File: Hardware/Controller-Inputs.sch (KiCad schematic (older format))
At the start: 35 parts, among them J1 RJ45, U1 PC817, U2 PC817, U3 PC817, U4 PC817, U5 PC817, U6 PC817, U8 74HC14

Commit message: Add files via upload
HW layout and libs
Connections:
- wire segments 116 -> 115
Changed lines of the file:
@@
 LIBS:L298N
 LIBS:WS2812B
+LIBS:a4973
 LIBS:a3968
 LIBS:lm2675
@@
 $EndComp
 $Comp
-L GND #PWR09
+L GND #PWR08
 U 1 1 5A67C8BB
 P 5050 6000
-F 0 "#PWR09" H 5050 5750 50  0001 C CNN
+F 0 "#PWR08" H 5050 5750 50  0001 C CNN
 F 1 "GND" H 5055 5827 50  0000 C CNN
 F 2 "" H 5050 6000 50  0001 C CNN
@@
 $EndComp
 $Comp
-L GND #PWR011
+L GND #PWR09
 U 1 1 5A67C8F8
 P 4550 6250
-F 0 "#PWR011" H 4550 6000 50  0001 C CNN
+F 0 "#PWR09" H 4550 6000 50  0001 C CNN
 F 1 "GND" H 4555 6077 50  0000 C CNN
 F 2 "" H 4550 6250 50  0001 C CNN
@@
 $EndComp
 $Comp
-L GND #PWR012
+L GND #PWR010
 U 1 1 5A67C90A
 P 6400 5150
-F 0 "#PWR012" H 6400 4900 50  0001 C CNN
+F 0 "#PWR010" H 6400 4900 50  0001 C CNN
 F 1 "GND" H 6405 4977 50  0000 C CNN
 F 2 "" H 6400 5150 50  0001 C CNN
@@
 $EndComp
 $Comp
-L GND #PWR013
+L GND #PWR011
 U 1 1 5A67C917
 P 6450 6350
-F 0 "#PWR013" H 6450 6100 50  0001 C CNN
+F 0 "#PWR011" H 6450 6100 50  0001 C CNN
 F 1 "GND" H 6455 6177 50  0000 C CNN
 F 2 "" H 6450 6350 50  0001 C CNN
@@
 U 1 1 5A67C930
 P 6200 5800
-F 0 "R15" V 6407 5800 50  0000 C CNN
-F 1 "10K" V 6316 5800 50  0000 C CNN
+F 0 "R15" V 6100 5800 50  0000 C CNN
+F 1 "10K" V 6200 5800 50  0000 C CNN
 F 2 "Resistors_SMD:R_0805_HandSoldering" V 6130 5800 50  0001 C CNN
 F 3 "" H 6200 5800 50  0001 C CNN
@@
 U 1 1 5A67C937
 P 6150 4600
-F 0 "R13" V 6357 4600 50  0000 C CNN
-F 1 "10K" V 6266 4600 50  0000 C CNN
+F 0 "R13" V 6050 4600 50  0000 C CNN
+F 1 "10K" V 6150 4600 50  0000 C CNN
 F 2 "Resistors_SMD:R_0805_HandSoldering" V 6080 4600 50  0001 C CNN
 F 3 "" H 6150 4600 50  0001 C CNN
@@
 $EndComp
 $Comp
-L GND #PWR014
+L GND #PWR012
 U 1 1 5A67D6AF
 P 4200 1850
-F 0 "#PWR014" H 4200 1600 50  0001 C CNN
+F 0 "#PWR012" H 4200 1600 50  0001 C CNN
 F 1 "GND" H 4205 1677 50  0000 C CNN
 F 2 "" H 4200 1850 50  0001 C CNN
@@
 $EndComp
 $Comp
-L GND #PWR016
+L GND #PWR013
 U 1 1 5A67D6C7
 P 5050 2900
-F 0 "#PWR016" H 5050 2650 50  0001 C CNN
+F 0 "#PWR013" H 5050 2650 50  0001 C CNN
 F 1 "GND" H 5055 2727 50  0000 C CNN
 F 2 "" H 5050 2900 50  0001 C CNN
@@
 $EndComp
 $Comp
-L GND #PWR018
+L GND #PWR014
 U 1 1 5A67D6FD
 P 4550 3150
-F 0 "#PWR018" H 4550 2900 50  0001 C CNN
+F 0 "#PWR014" H 4550 2900 50  0001 C CNN
 F 1 "GND" H 4555 2977 50  0000 C CNN
 F 2 "" H 4550 3150 50  0001 C CNN
@@
 $EndComp
 $Comp
-L GND #PWR019
+L GND #PWR015
 U 1 1 5A67D70E
 P 6400 2050
-F 0 "#PWR019" H 6400 1800 50  0001 C CNN
+F 0 "#PWR015" H 6400 1800 50  0001 C CNN
 F 1 "GND" H 6405 1877 50  0000 C CNN
 F 2 "" H 6400 2050 50  0001 C CNN
@@
 $EndComp
 $Comp
-L GND #PWR020
+L GND #PWR016
 U 1 1 5A67D71A
 P 6450 3250
-F 0 "#PWR020" H 6450 3000 50  0001 C CNN
+F 0 "#PWR016" H 6450 3000 50  0001 C CNN
 F 1 "GND" H 6455 3077 50  0000 C CNN
 F 2 "" H 6450 3250 50  0001 C CNN
@@
 $EndComp
 $Comp
-L GND #PWR022
+L GND #PWR017
 U 1 1 5A67D72C
 P 9200 3600
-F 0 "#PWR022" H 9200 3350 50  0001 C CNN
+F 0 "#PWR017" H 9200 3350 50  0001 C CNN
 F 1 "GND" H 9205 3427 50  0000 C CNN
 F 2 "" H 9200 3600 50  0001 C CNN
@@
 U 1 1 5A67D732
 P 6200 2700
-F 0 "R14" V 6407 2700 50  0000 C CNN
-F 1 "10K" V 6316 2700 50  0000 C CNN
+F 0 "R14" V 6100 2700 50  0000 C CNN
+F 1 "10K" V 6200 2700 50  0000 C CNN
 F 2 "Resistors_SMD:R_0805_HandSoldering" V 6130 2700 50  0001 C CNN
 F 3 "" H 6200 2700 50  0001 C CNN
@@
 U 1 1 5A67D738
 P 6150 1500
-F 0 "R12" V 6357 1500 50  0000 C CNN
-F 1 "10K" V 6266 1500 50  0000 C CNN
+F 0 "R12" V 6050 1500 50  0000 C CNN
+F 1 "10K" V 6150 1500 50  0000 C CNN
 F 2 "Resistors_SMD:R_0805_HandSoldering" V 6080 1500 50  0001 C CNN
 F 3 "" H 6150 1500 50  0001 C CNN
@@
 Connection ~ 4200 1500
 Wire Wire Line
-	2650 2500 4350 2500
+	1650 2500 4350 2500
 Wire Wire Line
 	4350 2500 4350 2550
@@
 	6850 1750 6850 1800
 $Comp
-L GNDD #PWR023
+L GNDD #PWR018
 U 1 1 5A69E1AB
 P 2550 1850
-F 0 "#PWR023" H 2550 1600 50  0001 C CNN
+F 0 "#PWR018" H 2550 1600 50  0001 C CNN
 F 1 "GNDD" H 2550 1725 50  0000 C CNN
 F 2 "" H 2550 1850 50  0001 C CNN
@@
 	4050 2850 3900 2850
 $Comp
-L GNDD #PWR024
+L GNDD #PWR019
 U 1 1 5A69E91D
 P 3400 2850
-F 0 "#PWR024" H 3400 2600 50  0001 C CNN
+F 0 "#PWR019" H 3400 2600 50  0001 C CNN
 F 1 "GNDD" H 3400 2725 50  0000 C CNN
 F 2 "" H 3400 2850 50  0001 C CNN
@@
 	3200 4900 2900 4900
 $Comp
-L GNDD #PWR025
+L GNDD #PWR020
 U 1 1 5A69F612
 P 2550 4950
-F 0 "#PWR025" H 2550 4700 50  0001 C CNN
+F 0 "#PWR020" H 2550 4700 50  0001 C CNN
 F 1 "GNDD" H 2550 4825 50  0000 C CNN
 F 2 "" H 2550 4950 50  0001 C CNN
@@
 	4050 5950 3750 5950
 $Comp
-L GNDD #PWR026
+L GNDD #PWR021
 U 1 1 5A69FED8
 P 3400 6000
-F 0 "#PWR026" H 3400 5750 50  0001 C CNN
+F 0 "#PWR021" H 3400 5750 50  0001 C CNN
 F 1 "GNDD" H 3400 5875 50  0000 C CNN
 F 2 "" H 3400 6000 50  0001 C CNN
@@
 	3400 5950 3400 6000
 Wire Wire Line
-	1650 2500 2600 2500
-Wire Wire Line
 	1550 2400 2100 2400
 Wire Wire Line
@@
 	1850 3450 1850 3700
 Wire Wire Line
-	1850 3700 1550 3700
-Text GLabel 1850 3700 2    60   Input ~ 0
+	1550 3700 2100 3700
+Text GLabel 2100 3700 2    60   Input ~ 0
 +24Logic
 Text GLabel 2200 6550 0    60   Input ~ 0
@@
 Wire Wire Line
 	2000 3900 2000 5500
-Connection ~ 2000 5500
 Wire Wire Line
 	1900 5700 1900 4000
@@
 	1900 4000 1550 4000
 $Comp
-L GNDD #PWR027
+L GNDD #PWR022
 U 1 1 5A6A1925
 P 1600 4200
-F 0 "#PWR027" H 1600 3950 50  0001 C CNN
+F 0 "#PWR022" H 1600 3950 50  0001 C CNN
 F 1 "GNDD" H 1600 4075 50  0000 C CNN
 F 2 "" H 1600 4200 50  0001 C CNN
@@
 $EndComp
 $Comp
-L +3.3V #PWR?
+L +3.3V #PWR023
 U 1 1 5A716CAE
 P 4200 1000
-F 0 "#PWR?" H 4200 850 50  0001 C CNN
+F 0 "#PWR023" H 4200 850 50  0001 C CNN
 F 1 "+3.3V" H 4200 1140 50  0000 C CNN
 F 2 "" H 4200 1000 50  0001 C CNN
@@
 $EndComp
 $Comp
-L +3.3V #PWR?
+L +3.3V #PWR024
 U 1 1 5A716D32
 P 5050 2050
-F 0 "#PWR?" H 5050 1900 50  0001 C CNN
+F 0 "#PWR024" H 5050 1900 50  0001 C CNN
 F 1 "+3.3V" H 5050 2190 50  0000 C CNN
 F 2 "" H 5050 2050 50  0001 C CNN
@@
 $EndComp
 $Comp
-L +3.3V #PWR?
+L +3.3V #PWR025
 U 1 1 5A717541
 P 9200 3300
-F 0 "#PWR?" H 9200 3150 50  0001 C CNN
+F 0 "#PWR025" H 9200 3150 50  0001 C CNN
 F 1 "+3.3V" H 9200 3440 50  0000 C CNN
 F 2 "" H 9200 3300 50  0001 C CNN
@@
 $EndComp
 $Comp
-L +3.3V #PWR?
+L +3.3V #PWR026
 U 1 1 5A7175BE
 P 4200 4100
-F 0 "#PWR?" H 4200 3950 50  0001 C CNN
+F 0 "#PWR026" H 4200 3950 50  0001 C CNN
 F 1 "+3.3V" H 4200 4240 50  0000 C CNN
 F 2 "" H 4200 4100 50  0001 C CNN
@@
 $EndComp
 $Comp
-L +3.3V #PWR?
+L +3.3V #PWR027
 U 1 1 5A71763B
 P 5050 5150
-F 0 "#PWR?" H 5050 5000 50  0001 C CNN
+F 0 "#PWR027" H 5050 5000 50  0001 C CNN
 F 1 "+3.3V" H 5050 5290 50  0000 C CNN
 F 2 "" H 5050 5150 50  0001 C CNN
@@
 $EndComp
 $Comp
-L GND #PWR?
+L GND #PWR028
 U 1 1 5A7190F0
 P 9200 4900
-F 0 "#PWR?" H 9200 4650 50  0001 C CNN
+F 0 "#PWR028" H 9200 4650 50  0001 C CNN
 F 1 "GND" H 9205 4727 50  0000 C CNN
 F 2 "" H 9200 4900 50  0001 C CNN
@@
 $EndComp
 $Comp
-L +3.3V #PWR?
+L +3.3V #PWR029
 U 1 1 5A71925A
 P 9200 4600
-F 0 "#PWR?" H 9200 4450 50  0001 C CNN
+F 0 "#PWR029" H 9200 4450 50  0001 C CNN
 F 1 "+3.3V" H 9200 4740 50  0000 C CNN
 F 2 "" H 9200 4600 50  0001 C CNN
@@
 Wire Wire Line
 	9200 4900 9200 4850
+Connection ~ 1850 3700
 $EndSCHEMATC

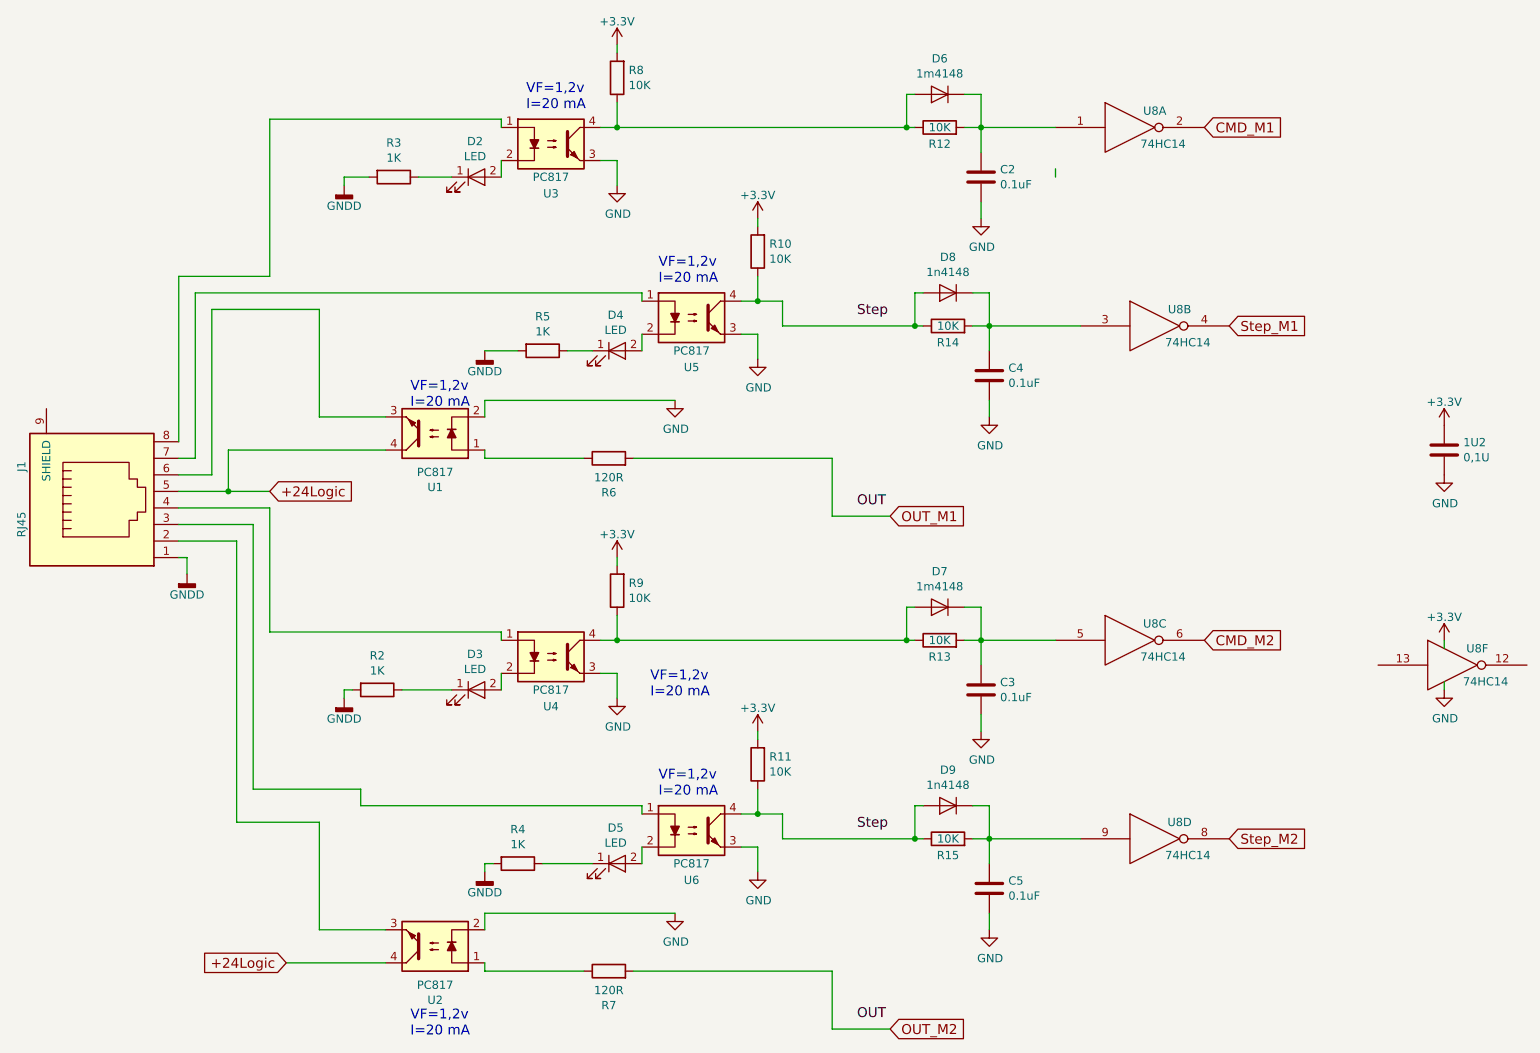
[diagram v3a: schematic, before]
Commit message: one motor
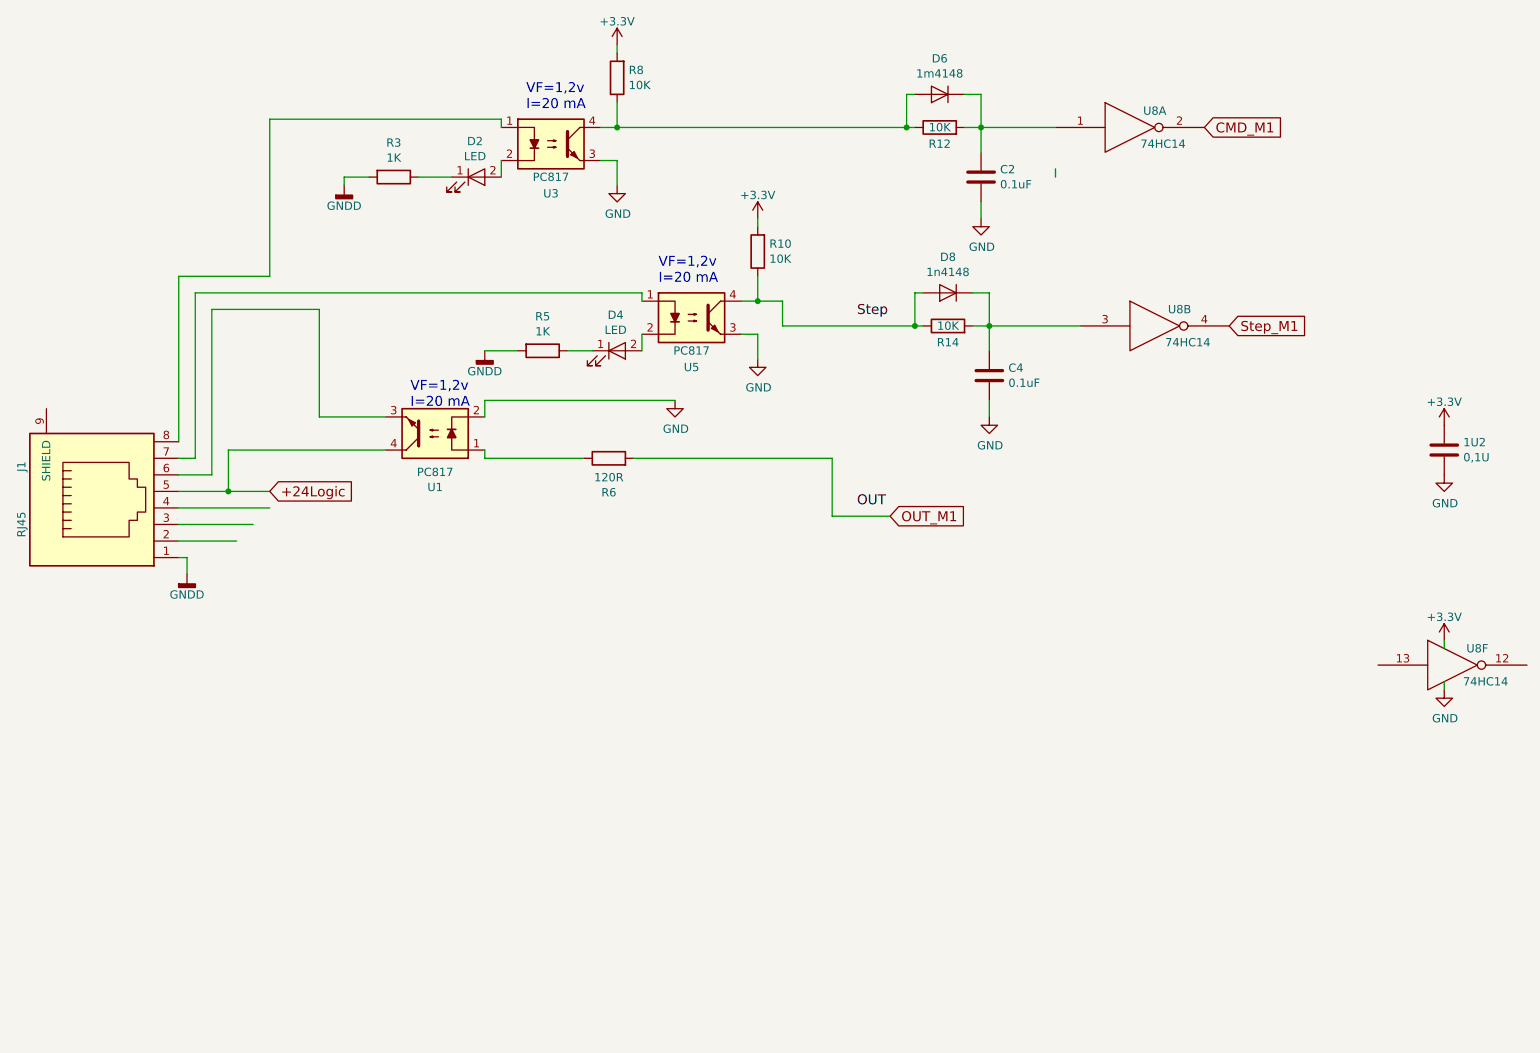
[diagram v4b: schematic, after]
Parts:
- removed C3, C5: 0.1uF, Capacitors_SMD:C_0805_HandSoldering, symbol C
- removed D3, D5: LED, LEDs:LED_0805_HandSoldering, symbol LED
- removed D7: 1m4148, Diodes_SMD:D_MiniMELF_Handsoldering, symbol D
- removed D9: 1n4148, Diodes_SMD:D_MiniMELF_Handsoldering, symbol D
- removed R11, R13, R15, R9: 10K, Resistors_SMD:R_0805_HandSoldering, symbol R
- removed R2, R4: 1K, Resistors_SMD:R_0805_HandSoldering, symbol R
- removed R7: 120R, Resistors_SMD:R_0805_HandSoldering, symbol R
- removed U2, U4, U6: PC817, Libs:817opto, symbol PC817
- removed unit 3 of U8
- removed unit 4 of U8
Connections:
- net labels removed: CMD_M2, OUT_M2, Step_M2
- wire segments 115 -> 63
